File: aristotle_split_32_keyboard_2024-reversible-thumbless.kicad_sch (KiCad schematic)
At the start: 39 parts, among them J1 8P8C, J2 Screw_Terminal_01x04, J3 Screw_Terminal_01x04, K13 SW_SPDT, K14 SW_SPDT, K15 SW_SPDT, K16 SW_SPDT, K17 SW_SPDT, K23 SW_SPDT, K24 SW_SPDT, K25 SW_SPDT, K26 SW_SPDT, K27 SW_SPDT, K4 SW_SPDT, K5 SW_SPDT, K6 SW_SPDT, K7 SW_SPDT, SW1 SW_SPDT, U1 ProMicro_r

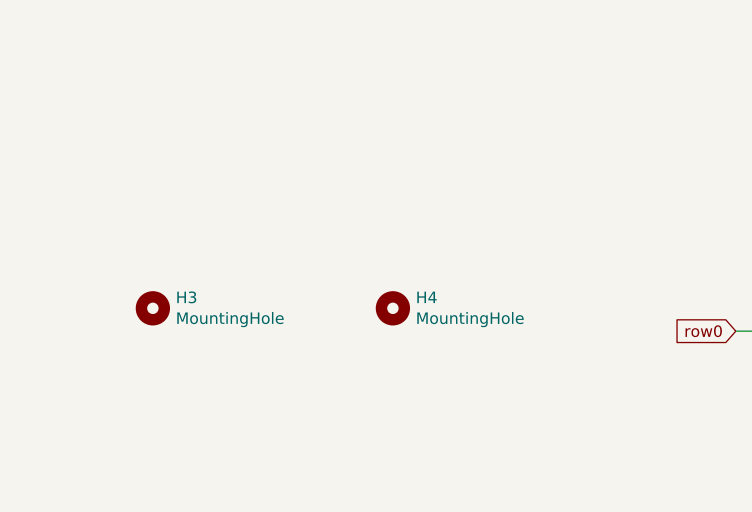
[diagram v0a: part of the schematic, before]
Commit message: Fix mounting holes
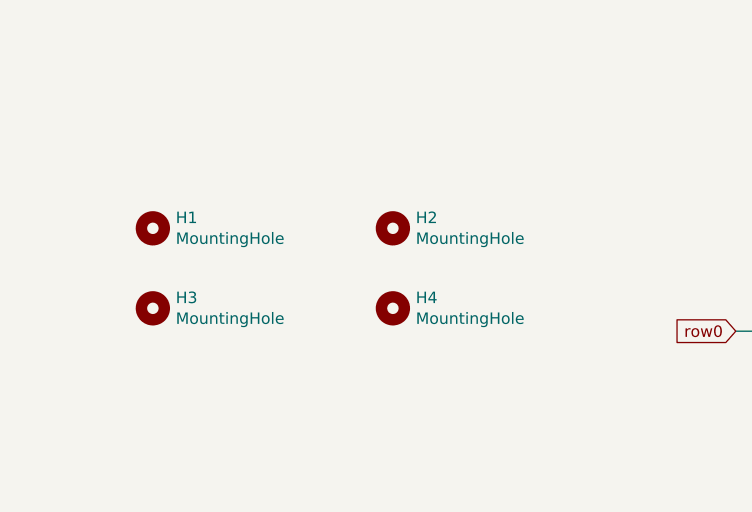
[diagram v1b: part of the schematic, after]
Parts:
- added H1, H2: MountingHole, MountingHole:MountingHole_2.2mm_M2, symbol Mechanical:MountingHole
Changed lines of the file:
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@@
+    )
+  )
+  (symbol (lib_id "Mechanical:MountingHole") (at 29.21 58.42 0) (unit 1)
+    (in_bom yes) (on_board yes) (dnp no)
+    (property "Reference" "H1" (at 31.75 57.2516 0)
+      (effects (font (size 1.27 1.27)) (justify left))
+    )
+    (property "Value" "MountingHole" (at 31.75 59.563 0)
+      (effects (font (size 1.27 1.27)) (justify left))
+    )
+    (property "Footprint" "MountingHole:MountingHole_2.2mm_M2" (at 29.21 58.42 0)
+      (effects (font (size 1.27 1.27)) hide)
+    )
+    (property "Datasheet" "~" (at 29.21 58.42 0)
+      (effects (font (size 1.27 1.27)) hide)
+    )
+    (instances
+      (project "aristotle_split_32_keyboard_2024-reversible-thumbless"
+        (path "/31e08896-1992-4725-96d9-9d2728bca7a3"
+          (reference "H1") (unit 1)
+        )
+      )
     )
   )
@@
         )
       )
+    )
+  )
+  (symbol (lib_id "Mechanical:MountingHole") (at 55.88 58.42 0) (unit 1)
+    (in_bom yes) (on_board yes) (dnp no)
+    (property "Reference" "H2" (at 58.42 57.2516 0)
+      (effects (font (size 1.27 1.27)) (justify left))
+    )
+    (property "Value" "MountingHole" (at 58.42 59.563 0)
+      (effects (font (size 1.27 1.27)) (justify left))
+    )
+    (property "Footprint" "MountingHole:MountingHole_2.2mm_M2" (at 55.88 58.42 0)
+      (effects (font (size 1.27 1.27)) hide)
+    )
+    (property "Datasheet" "~" (at 55.88 58.42 0)
+      (effects (font (size 1.27 1.27)) hide)
+    )
+    (instances
+      (project "aristotle_split_32_keyboard_2024-reversible-thumbless"
+        (path "/31e08896-1992-4725-96d9-9d2728bca7a3"
+          (reference "H2") (unit 1)
+        )
+      )

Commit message: More rerouting
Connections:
- net at J2.2 (Pin_2), J3.3 (Pin_3): now also D31.2 (A); no longer D30.2 (A)
- net at J2.3 (Pin_3), J3.2 (Pin_2): now also D30.2 (A); no longer D31.2 (A)
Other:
- moved on the sheet: D30, D31

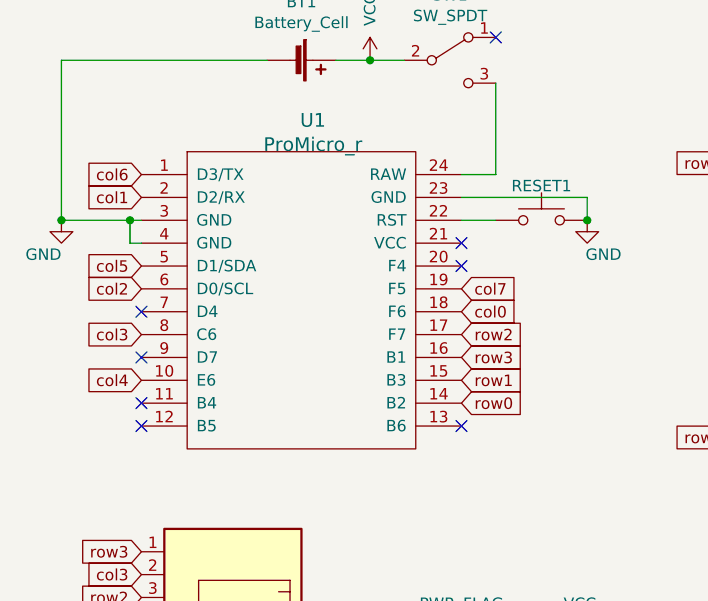
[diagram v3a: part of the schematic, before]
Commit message: Reassign MCU pins to rows/columns
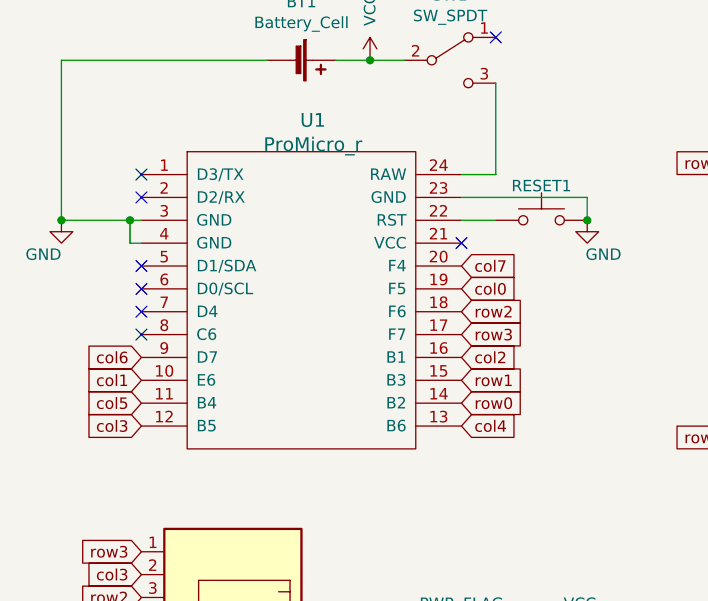
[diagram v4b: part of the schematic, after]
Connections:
- net col0: now also U1.19 (F5); no longer U1.18 (F6)
- net col1: now also U1.10 (E6); no longer U1.2 (D2/RX)
- net col2: now also U1.16 (B1); no longer U1.6 (D0/SCL)
- net col3: now also U1.12 (B5); no longer U1.8 (C6)
- net col4: now also U1.13 (B6); no longer U1.10 (E6)
- net col5: now also U1.11 (B4); no longer U1.5 (D1/SDA)
- net col6: now also U1.9 (D7); no longer U1.1 (D3/TX)
- net col7: now also U1.20 (F4); no longer U1.19 (F5)
- net row2: now also U1.18 (F6); no longer U1.17 (F7)
- net row3: now also U1.17 (F7); no longer U1.16 (B1)

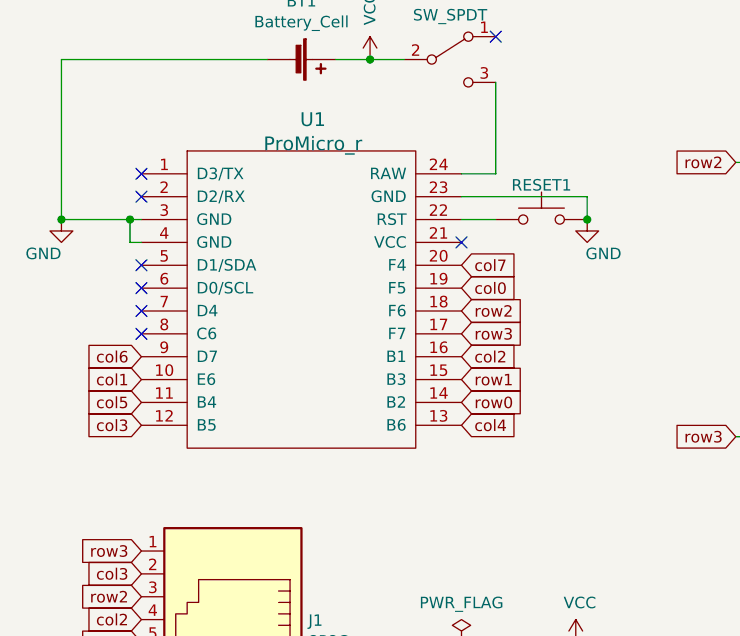
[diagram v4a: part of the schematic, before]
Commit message: Move pins; update symbol library with pin numbers
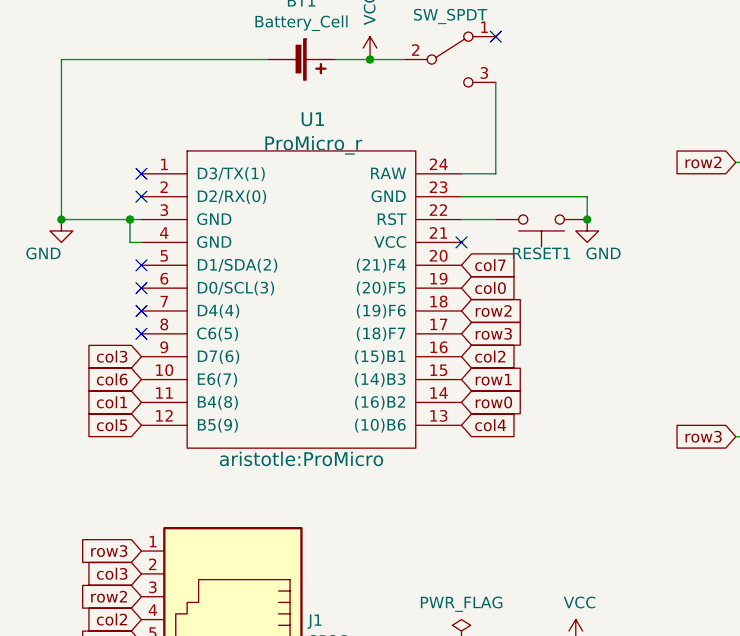
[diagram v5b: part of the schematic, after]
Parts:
- U1: symbol promicro:ProMicro -> aristotle-promicro:ProMicro
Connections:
- net GND: now also RESET1.1; no longer RESET1.2
- net col1: now also U1.11 (B4(8)); no longer U1.10 (E6)
- net col3: now also U1.9 (D7(6)); no longer U1.12 (B5)
- net col5: now also U1.12 (B5(9)); no longer U1.11 (B4)
- net col6: now also U1.10 (E6(7)); no longer U1.9 (D7)
- net at U1.22 (RST): now also RESET1.2; no longer RESET1.1
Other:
- moved on the sheet: RESET1
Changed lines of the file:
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@@
     )
   )
-  (global_label "col6" (shape input) (at 27.94 151.13 180) (fields_autoplaced)
-    (effects (font (size 1.27 1.27)) (justify right))
-    (property "Intersheetrefs" "${INTERSHEET_REFS}" (at 90.17 303.53 0)
+  (global_label "col6" (shape input) (at 27.94 153.67 180) (fields_autoplaced)
+    (effects (font (size 1.27 1.27)) (justify right))
+    (property "Intersheetrefs" "${INTERSHEET_REFS}" (at 90.17 306.07 0)
       (effects (font (size 1.27 1.27)) hide)
     )
@@
     )
   )
-  (global_label "col3" (shape input) (at 27.94 158.75 180) (fields_autoplaced)
-    (effects (font (size 1.27 1.27)) (justify right))
-    (property "Intersheetrefs" "${INTERSHEET_REFS}" (at 21.5034 158.6706 0)
+  (global_label "col3" (shape input) (at 27.94 151.13 180) (fields_autoplaced)
+    (effects (font (size 1.27 1.27)) (justify right))
+    (property "Intersheetrefs" "${INTERSHEET_REFS}" (at 21.5034 151.0506 0)
       (effects (font (size 1.27 1.27)) (justify right) hide)
     )
@@
     )
   )
-  (global_label "col1" (shape input) (at 27.94 153.67 180) (fields_autoplaced)
-    (effects (font (size 1.27 1.27)) (justify right))
-    (property "Intersheetrefs" "${INTERSHEET_REFS}" (at 21.5034 153.5906 0)
+  (global_label "col1" (shape input) (at 27.94 156.21 180) (fields_autoplaced)
+    (effects (font (size 1.27 1.27)) (justify right))
+    (property "Intersheetrefs" "${INTERSHEET_REFS}" (at 21.5034 156.1306 0)
       (effects (font (size 1.27 1.27)) (justify right) hide)
     )
@@
     )
   )
-  (global_label "col5" (shape input) (at 27.94 156.21 180) (fields_autoplaced)
-    (effects (font (size 1.27 1.27)) (justify right))
-    (property "Intersheetrefs" "${INTERSHEET_REFS}" (at 90.17 306.07 0)
+  (global_label "col5" (shape input) (at 27.94 158.75 180) (fields_autoplaced)
+    (effects (font (size 1.27 1.27)) (justify right))
+    (property "Intersheetrefs" "${INTERSHEET_REFS}" (at 90.17 308.61 0)
       (effects (font (size 1.27 1.27)) hide)
     )
@@
     )
   )
-  (symbol (lib_id "promicro:ProMicro") (at 45.72 149.86 0) (unit 1)
+  (symbol (lib_id "aristotle-promicro:ProMicro") (at 45.72 149.86 0) (unit 1)
     (in_bom yes) (on_board yes) (dnp no)
     (property "Reference" "U1" (at 46.99 124.7902 0)
@@
       (effects (font (size 1.524 1.524)))
     )
-    (property "Footprint" "aristotle:ProMicro" (at 49.53 176.53 0)
-      (effects (font (size 1.524 1.524)) hide)
-    )
-    (property "Datasheet" "" (at 49.53 176.53 0)
+    (property "Footprint" "aristotle:ProMicro" (at 45.72 162.56 0)
+      (effects (font (size 1.524 1.524)))
+    )
+    (property "Datasheet" "" (at 48.26 176.53 0)
       (effects (font (size 1.524 1.524)))
     )
@@
     )
   )
-  (symbol (lib_id "Switch:SW_Push") (at 72.39 135.89 0) (unit 1)
-    (in_bom yes) (on_board yes) (dnp no)
-    (property "Reference" "RESET1" (at 72.39 132.08 0)
-      (effects (font (size 1.27 1.27)))
-    )
-    (property "Value" "~" (at 72.39 131.7244 0)
-      (effects (font (size 1.27 1.27)))
-    )
-    (property "Footprint" "aristotle:SW_PUSH_6mm" (at 72.39 130.81 0)
-      (effects (font (size 1.27 1.27)) hide)
-    )
-    (property "Datasheet" "~" (at 72.39 130.81 0)
-      (effects (font (size 1.27 1.27)) hide)
-    )
+  (symbol (lib_id "Switch:SW_Push") (at 72.39 135.89 180) (unit 1)
+    (in_bom yes) (on_board yes) (dnp no)
+    (property "Reference" "RESET1" (at 72.39 139.7 0)
+      (effects (font (size 1.27 1.27)))
+    )
+    (property "Value" "~" (at 72.39 140.0556 0)
+      (effects (font (size 1.27 1.27)))
+    )
+    (property "Footprint" "aristotle:SW_PUSH_6mm" (at 72.39 140.97 0)
+      (effects (font (size 1.27 1.27)) hide)
+    )
+    (property "Datasheet" "~" (at 72.39 140.97 0)
+      (effects (font (size 1.27 1.27)) hide)
+    )
